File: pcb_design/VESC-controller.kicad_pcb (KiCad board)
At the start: 4 copper layers, 160 x 90 mm, 319 parts, among them J1 GATE_DRIVER_CONN_U, J2 GATE_DRIVER_CONN_V, J3 GATE_DRIVER_CONN_W, J4 micro USB, J5 ACCEL, J6 REGEN, J7 12V, J8 V_BUS, J9 SWD, P1 HALL/Encoder, P101 CANBUS, P2 Resolver, P3 PWR_COMM, Q1 BSC340N08, Q2 2N7002PW, Q3 AO4805, SW1 BOOTLOADER, U1 STM32F40X_LQFP64, U10 LM2903-SO8, U11 LM3488, U12 OPA2376AID, U13 LM1117IMP-v.v, U14 OPA2376AID, U15 AD2S1205, U16 OPA2376AID, U17 LM2903-SO8, U18 AND3, U19 AD8397, U2 ISO1050, U20 APX809, U21 NCV78Mxx, U3 OPA2376AID, U4 LM2903-SO8, U5 7400-TSSOP, U6 SN74ACT08PWR, U7 SN74ACT08PWR, U8 SN74AUP1G74, U9 LM22676QTJ-5.0, X1 ABM3B - 8MHz, X2 ABM3B - 8MHz

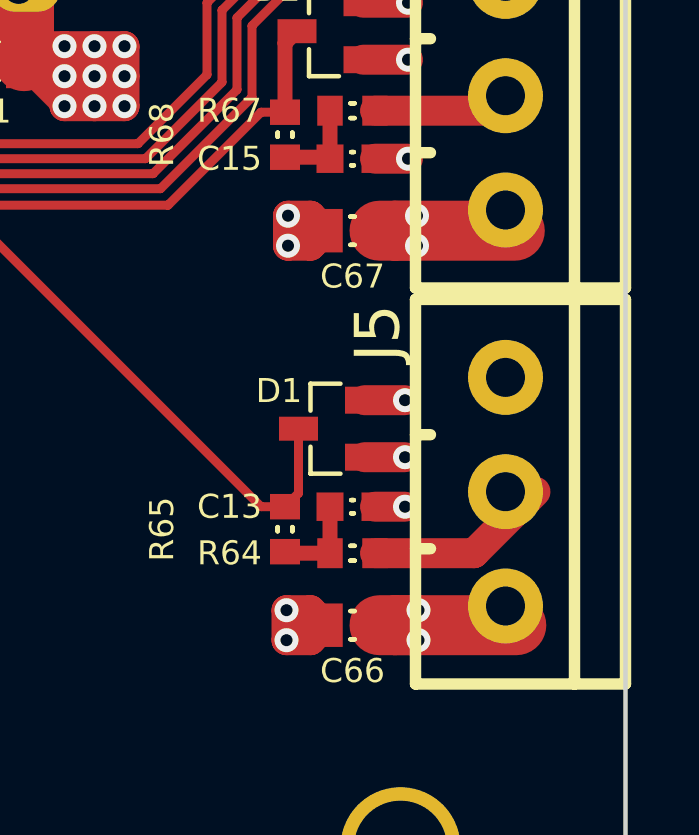
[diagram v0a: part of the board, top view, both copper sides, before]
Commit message: Updated component values according to simulations. 1.5khz for user inputs and  240khz lp pass filters for motor control
Signed-off-by: Marcos Chaparro <mchaparro@paltatech.com>
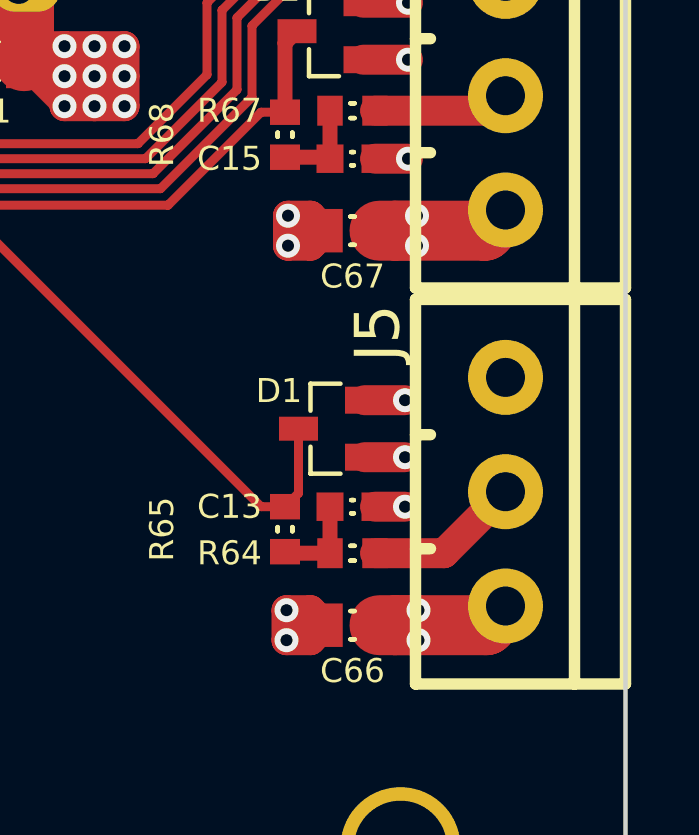
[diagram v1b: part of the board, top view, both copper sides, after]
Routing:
- net /Accel input conditioning/IN: track 6.20 -> 5.20 mm
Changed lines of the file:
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@@
     (thickness 1.6)
     (drawings 74)
-    (tracks 4755)
+    (tracks 4757)
     (zones 0)
     (modules 319)
@@
     (0 F.Cu signal)
     (1 GND.Cu signal)
-    (2 PWR.Cu signal hide)
+    (2 PWR.Cu signal)
     (31 B.Cu signal)
     (32 B.Adhes user)
@@
   )
   (setup
-    (last_trace_width 0.19)
+    (last_trace_width 2)
     (user_trace_width 0.2)
     (user_trace_width 0.25)
@@
   (segment (start 29.25 -1.95) (end 29.25 -2.925) (width 0.25) (layer F.Cu) (net 105))
   (segment (start 29.25 -2.925) (end 29.475 -3.15) (width 0.25) (layer F.Cu) (net 105))
-  (segment (start 71.65 27.7) (end 74.95 27.7) (width 1) (layer F.Cu) (net 106))
-  (segment (start 74.95 27.7) (end 77 25.65) (width 1) (layer F.Cu) (net 106))
+  (segment (start 71.65 27.7) (end 73.95 27.7) (width 1) (layer F.Cu) (net 106))
+  (segment (start 73.95 27.7) (end 76 25.65) (width 1) (layer F.Cu) (net 106))
   (segment (start 71.65 12.95) (end 76.5 12.95) (width 1) (layer F.Cu) (net 107))
   (segment (start 28.7 40.8) (end 28.7 38.475) (width 0.3) (layer F.Cu) (net 108) (status 10))
@@
   (segment (start 20.2 -36.8) (end 19.5 -36.1) (width 3) (layer F.Cu) (net 132))
   (segment (start 22.45 -34.2) (end 22.45 -36.8) (width 3) (layer F.Cu) (net 132))
+  (segment (start 71.8 30.1) (end 75.36 30.1) (width 2) (layer F.Cu) (net 133))
+  (segment (start 75.36 30.1) (end 76 29.46) (width 2) (layer F.Cu) (net 133))
+  (segment (start 71.8 16.95) (end 75.31 16.95) (width 2) (layer F.Cu) (net 133))
+  (segment (start 75.31 16.95) (end 76 16.26) (width 2) (layer F.Cu) (net 133))
   (segment (start 70.397745 -32.284414) (end 77.965586 -32.284414) (width 2) (layer F.Cu) (net 133))
   (segment (start 77.965586 -32.284414) (end 78.600001 -31.649999) (width 2) (layer F.Cu) (net 133))
@@
   (via (at 26.9 34.6) (size 0.8) (drill 0.4) (layers F.Cu B.Cu) (net 133))
   (via (at 27.9 34.6) (size 0.8) (drill 0.4) (layers F.Cu B.Cu) (net 133))
-  (segment (start 71.8 16.95) (end 76.31 16.95) (width 2) (layer F.Cu) (net 133))
-  (segment (start 71.8 30.1) (end 76.36 30.1) (width 2) (layer F.Cu) (net 133))
   (segment (start 73.05 16.45) (end 73.05 17.45) (width 1) (layer F.Cu) (net 133))
   (segment (start 73.05 16.45) (end 73.615685 16.45) (width 1) (layer PWR.Cu) (net 133))

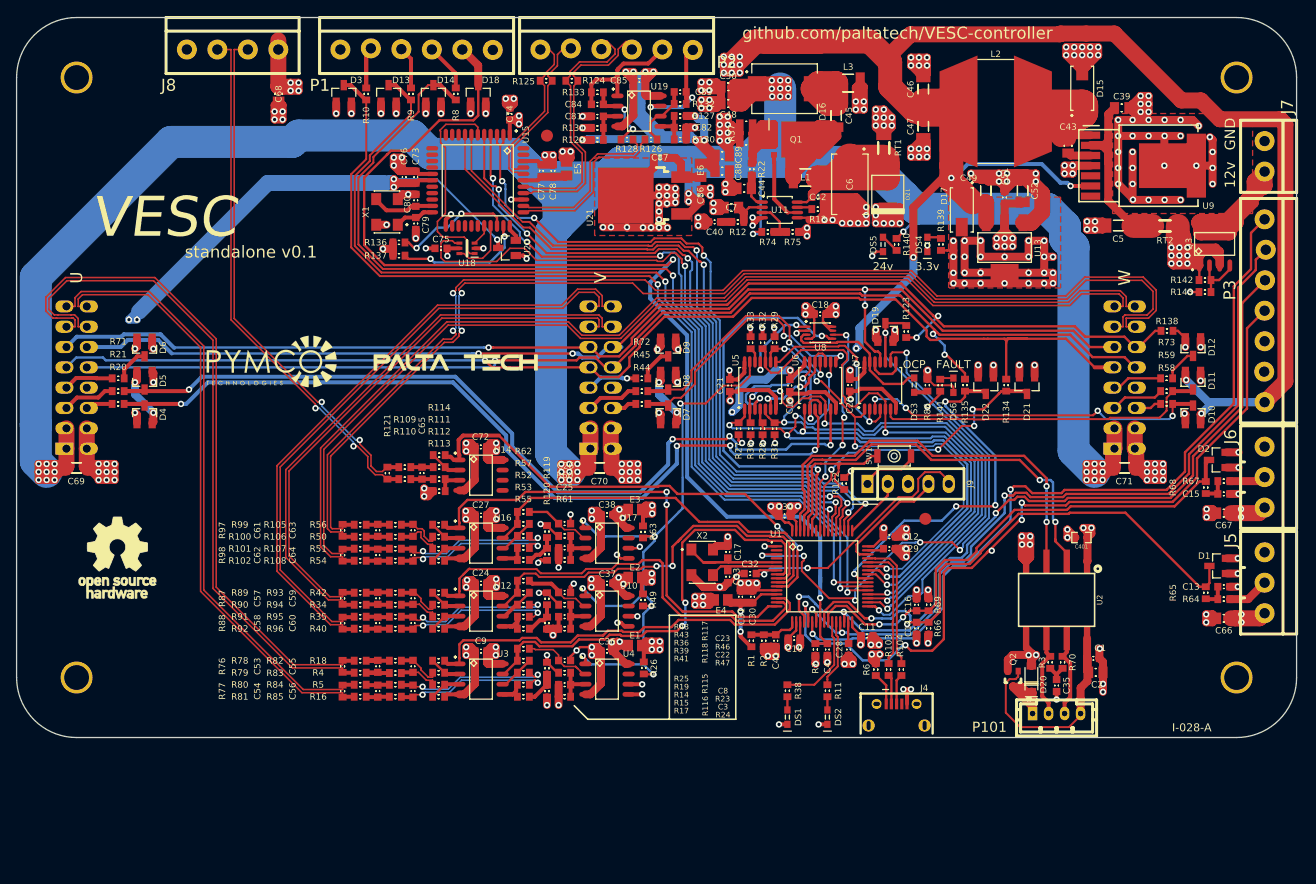
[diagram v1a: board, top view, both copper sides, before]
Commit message: Corrected phase current gain. More 3d models
Signed-off-by: Marcos Chaparro <mchaparro@paltatech.com>
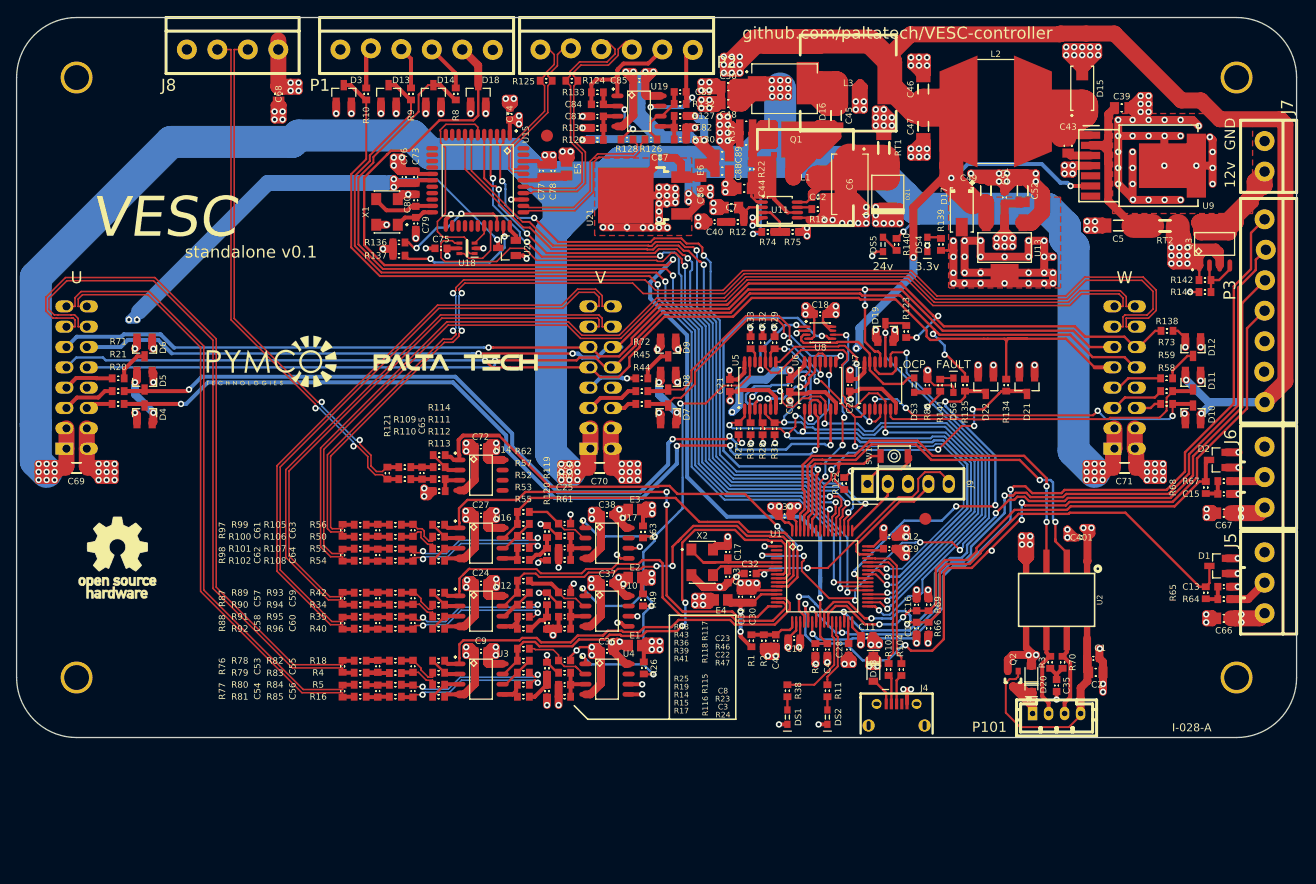
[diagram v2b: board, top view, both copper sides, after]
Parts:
- removed R6: 0R, IPC7351-Nominal:RESC1608X50
- added D23: MBR0540, smd-semi:SOD-123, F.Cu at (27.1, 36.4)
- C10, C11, C12, C34: value 2.2u -> 100nF
- C13, C15: value 1nF -> 100nF
- C17, C33, C79, C80: value 15p -> 15pF
- C2: value 10uF -> 4.7uF
- C28, C29, C31, C41: value 2.2u -> 2.2uF
- C32: value 100n -> 100nF
- C4: value 4.7nF -> 2.2uF
- C401: value 2.2u -> 100nF; footprint CRF1:SMD-0603_c -> IPC7351-Nominal:CAPC1608X55
- C5: value 10uF 50v -> 10uF 35v
- C53, C54, C57, C58, C61, C62: value 100pF -> 2.2nF
- C55, C56, C59, C60, C63, C64: value 100pF -> 220pF
- C6: value 4.7uF 50v -> 4.7uF 50v tant
- C76, C78: value 4.7uF -> 2.2uF
- E4: value BEAD-0805 -> BEAD-220ohm@100khz
- L1, L3: value L-1210 -> 22uH 5.2A; footprint IPC7351-Nominal:INDC3225X135 -> manuf:BOURNS-SRR1210
- R105, R106, R107, R108, R64, R67, R82, R83, R84, R85, R93, R94, R95, R96: value 100R -> 1k
- R109, R110: value 100R -> 4.7k
- R124, R125: value 68k -> 68.1k
- R14, R15, R34, R35, R36, R39, R4, R5, R50, R51, R52, R53: value 10k -> 8.87k
- R16, R40, R54: value R-0603 -> 10k
- R17, R41, R55: value 9.5k -> 10k
- R3, R70: value 120R -> 60.4R
- R65, R68: value 5.2k -> 100k
- R66, R69: value 10k -> 270k
- RT1: value POLYFUSE 5A -> FUSE 5A SLOW
- RT2: value POLYFUSE- 2A -> POLYFUSE 1A
- SW1: footprint paltatech:SMD-Switch_B3U-1000-B -> SMD-Switch_B3U-1000-B
- U10, U17, U4: value LM2903-SO8 -> LM2903DT
- U12, U14, U16, U3: value OPA2376AID -> OPA2376AIDR
- U18: value AND3 -> SN74LVC1G
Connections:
- net /conditioning U/OC_Fault renamed /conditioning U/~OC_Fault
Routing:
- net +5: track 682.1 -> 437.3 mm, vias 41 -> 27
- net GND: track 724.7 -> 951.5 mm, vias 286 -> 296
- net (no net): track 0.00 -> 12.5 mm, vias 0 -> 4
- net Net-(C45-Pad2): track 40.0 -> 48.0 mm
- net Net-(Q1-Pad4): track 9.16 -> 1.18 mm
- net Net-(C42-Pad1): track 25.3 -> 29.2 mm
- net Net-(D23-Pad2): track 4.13 -> 3.59 mm

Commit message: Fixed power supply inductor footprints in the layout
Signed-off-by: Marcos Chaparro <mchaparro@paltatech.com>
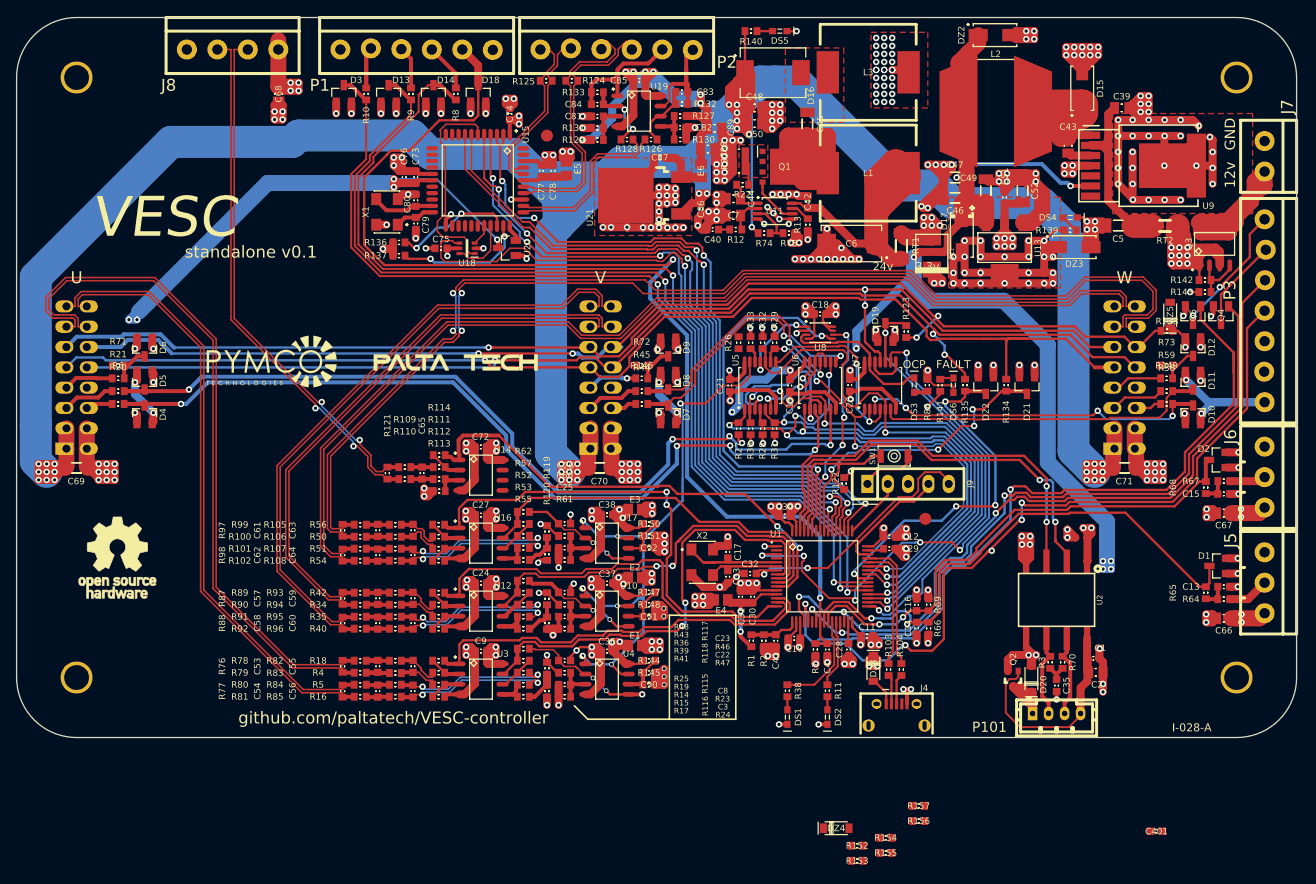
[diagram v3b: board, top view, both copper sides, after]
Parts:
- removed R49, R63: 4.7k, IPC7351-Nominal:RESC1608X50
- added C90: 100nF, IPC7351-Nominal:CAPC1608X55, F.Cu at (-0.95, 38.4)
- added C91: 100nF, IPC7351-Nominal:CAPC1608X55, F.Cu at (-0.95, 29.9)
- added C92: 100nF, IPC7351-Nominal:CAPC1608X55, F.Cu at (-0.95, 21.3)
- added DZ2: 5.7v zener, IPC7351-Nominal:DIOM5226X203, F.Cu at (42.3, -42.8)
- added DZ3: 4v zener, IPC7351-Nominal:DIOM5226X203, F.Cu at (52.2, -16.3)
- added DZ4: MMSZ52XXB, smd-semi:SOD-123, F.Cu at (22.4, 56.3)
- added DZ5: MMSZ52XXB, smd-semi:SOD-123, F.Cu at (64.2, -7.80)
- added Q4: SI2302, smd-semi:SOT-23, F.Cu at (70.5, -7.80)
- added Q5: SI2302, smd-semi:SOT-23, F.Cu at (67.0, -7.80)
- added R144: 10k, IPC7351-Nominal:RESC1608X50, F.Cu at (-0.95, 35.4)
- added R145: 1k, IPC7351-Nominal:RESC1608X50, F.Cu at (-0.95, 36.9)
- added R146: 10k, IPC7351-Nominal:RESC1608X50, F.Cu at (-1.85, -1.50)
- added R147: 10k, IPC7351-Nominal:RESC1608X50, F.Cu at (-0.95, 26.9)
- added R148: 1k, IPC7351-Nominal:RESC1608X50, F.Cu at (-0.95, 28.4)
- added R149: 10k, IPC7351-Nominal:RESC1608X50, F.Cu at (63.8, -1.50)
- added R150: 10k, IPC7351-Nominal:RESC1608X50, F.Cu at (-0.95, 18.3)
- added R151: 1k, IPC7351-Nominal:RESC1608X50, F.Cu at (-0.95, 19.8)
- added R152: 1k, IPC7351-Nominal:RESC1608X50, F.Cu at (25.1, 58.5)
- added R153: 1k, IPC7351-Nominal:RESC1608X50, F.Cu at (25.1, 60.4)
- added R154: NI, IPC7351-Nominal:RESC1608X50, F.Cu at (28.6, 57.5)
- added R155: NI, IPC7351-Nominal:RESC1608X50, F.Cu at (28.6, 59.4)
- added R156: NI, IPC7351-Nominal:RESC1608X50, F.Cu at (32.8, 55.4)
- added R157: NI, IPC7351-Nominal:RESC1608X50, F.Cu at (32.8, 53.5)
- added R6: 10k, IPC7351-Nominal:RESC1608X50, F.Cu at (-67.3, -1.50)
- DS5: value RED -> GREEN
- R113, R114: value 10k -> 22k
- R14, R15, R36, R39, R52, R53: value 8.87k -> 10k
- R17, R19, R41, R43, R55, R57: value 10k -> 8.87k
- R34, R35, R4, R5, R50, R51: value 8.87k -> 5.6k
- SW1: footprint SMD-Switch_B3U-1000-B -> paltatech:SMD-Switch_B3U-1000-B
- moved R26 42.3 mm to (10.2, -4.35), turned to 270 degrees
- moved C401 37.9 mm to (62.5, 56.7), turned to 0 degrees
- moved R140 32.3 mm to (11.8, -43.3), turned to 180 degrees
- moved DS5 29.6 mm to (15.4, -43.3), turned to 180 degrees
- moved DS4 18.2 mm to (51.7, -20.0), turned to 180 degrees
- moved R139 16.2 mm to (51.7, -18.4), turned to 180 degrees
- moved C46 14.2 mm to (37.3, -22.4), turned to 180 degrees
- moved RT1 12.4 mm to (30.6, -16.4)
- moved DZ1 9.21 mm to (34.4, -15.5)
- moved L1 7.87 mm to (26.4, -25.6)
- moved C47 7.53 mm to (37.3, -25.0), turned to 180 degrees
- moved C6 7.40 mm to (24.4, -16.8), turned to 180 degrees
- moved C50 5.66 mm to (12.2, -31.8), turned to 0 degrees
- moved C45 3.75 mm to (18.9, -31.7)
- moved Q1 3.69 mm to (16.0, -26.4)
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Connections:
- net /conditioning U/Power_good renamed /conditioning U/TEMP_G
- net /conditioning V/Power_good renamed /conditioning V/TEMP_G
- net /conditioning W/Power_good renamed /conditioning W/TEMP_G
- D12 pad 3: Net-(D12-Pad3) -> /conditioning W/TEMP
- D6 pad 3: Net-(D6-Pad3) -> /conditioning U/TEMP
- D9 pad 3: Net-(D9-Pad3) -> /conditioning V/TEMP
- DZ1 pad 1: Net-(C42-Pad1) -> Net-(DZ1-Pad1)
- P3 pad 1: /STM32F4/MISO_ADC_EXT2 -> /Protected GPIOs/OUT2
- P3 pad 2: /STM32F4/TX_SCL_MOSI -> /Protected GPIOs/OUT1
- P3 pad 3: /STM32F4/RX_SDA_NSS -> /STM32F4/TX_SCL_MOSI
- P3 pad 4: /STM32F4/SCK_ADC_EXT -> /STM32F4/RX_SDA_NSS
- Q3 pad 1: Net-(Q3-Pad1) -> Net-(DZ1-Pad1)
- Q3 pad 3: Net-(Q3-Pad1) -> Net-(DZ1-Pad1)
- R100 pad 2: /conditioning W/V_phase- -> /conditioning W/V_phase+
- R101 pad 2: /conditioning W/I_phase+ -> /conditioning W/I_phase-
- R102 pad 2: /conditioning W/I_phase- -> /conditioning W/I_phase+
- R109 pad 2: /V_bus+ -> /V_bus-
- R110 pad 2: /V_bus- -> /V_bus+
- R121 pad 1: /V_bus- -> /V_bus+
- R121 pad 2: /V_bus+ -> /V_bus-
- R142 pad 2: Net-(Q3-Pad1) -> Net-(DZ1-Pad1)
- R26 pad 1: /conditioning U/~OC_Fault -> +3.3
- R26 pad 2: +3.3 -> /conditioning U/~OC_Fault
- R71 pad 1: Net-(D6-Pad3) -> /conditioning U/TEMP
- R72 pad 1: Net-(D9-Pad3) -> /conditioning V/TEMP
- R73 pad 1: Net-(D12-Pad3) -> /conditioning W/TEMP
- R76 pad 1: /conditioning U/V_phase- -> /conditioning U/V_phase+
- R76 pad 2: /conditioning U/V_phase+ -> /conditioning U/V_phase-
- R77 pad 1: /conditioning U/I_phase- -> /conditioning U/I_phase+
- R77 pad 2: /conditioning U/I_phase+ -> /conditioning U/I_phase-
- R78 pad 2: /conditioning U/V_phase+ -> /conditioning U/V_phase-
- R79 pad 2: /conditioning U/V_phase- -> /conditioning U/V_phase+
- R80 pad 2: /conditioning U/I_phase+ -> /conditioning U/I_phase-
- R81 pad 2: /conditioning U/I_phase- -> /conditioning U/I_phase+
- R87 pad 1: /conditioning V/V_phase- -> /conditioning V/V_phase+
- R87 pad 2: /conditioning V/V_phase+ -> /conditioning V/V_phase-
- R88 pad 1: /conditioning V/I_phase- -> /conditioning V/I_phase+
- R88 pad 2: /conditioning V/I_phase+ -> /conditioning V/I_phase-
- R89 pad 2: /conditioning V/V_phase+ -> /conditioning V/V_phase-
- R90 pad 2: /conditioning V/V_phase- -> /conditioning V/V_phase+
- R91 pad 2: /conditioning V/I_phase+ -> /conditioning V/I_phase-
- R92 pad 2: /conditioning V/I_phase- -> /conditioning V/I_phase+
- R97 pad 1: /conditioning W/V_phase- -> /conditioning W/V_phase+
- R97 pad 2: /conditioning W/V_phase+ -> /conditioning W/V_phase-
- R98 pad 1: /conditioning W/I_phase- -> /conditioning W/I_phase+
- R98 pad 2: /conditioning W/I_phase+ -> /conditioning W/I_phase-
- R99 pad 2: /conditioning W/V_phase+ -> /conditioning W/V_phase-
- RT1 pad 2: Net-(Q3-Pad1) -> Net-(DZ1-Pad1)
- RT2 pad 2: Net-(Q3-Pad1) -> Net-(DZ1-Pad1)
- U1 pad 20: /STM32F4/RX_SDA_NSS -> /conditioning U/TEMP
- U1 pad 21: /STM32F4/SCK_ADC_EXT -> /conditioning V/TEMP
- U1 pad 22: /STM32F4/MISO_ADC_EXT2 -> /conditioning W/TEMP
- U1 pad 23: /STM32F4/TX_SCL_MOSI -> /Protected GPIOs/IN2
- U1 pad 58: /STM32F4/PWM_AUX -> /Protected GPIOs/IN1
- U10 pad 5: GND -> Net-(C23-Pad1)
- U10 pad 6: +3.3 -> Net-(C91-Pad1)
- U10 pad 7: Net-(U10-Pad7) -> /conditioning U/~OC_Fault
- U17 pad 5: GND -> Net-(C26-Pad1)
- U17 pad 6: +3.3 -> Net-(C92-Pad1)
- U17 pad 7: Net-(U17-Pad7) -> /conditioning U/~OC_Fault
- U4 pad 5: GND -> Net-(C8-Pad1)
- U4 pad 6: +3.3 -> Net-(C90-Pad1)
- U4 pad 7: Net-(U4-Pad7) -> /conditioning U/~OC_Fault
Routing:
- net GND: track 951.5 -> 745.6 mm, vias 296 -> 325
- net +5: track 437.3 -> 636.7 mm, vias 27 -> 36
- net Net-(DZ1-Pad1): track 0.00 -> 108.8 mm, vias 0 -> 14
- net Net-(Q3-Pad1): track 100.3 -> 0.00 mm, vias 17 -> 0
- net /STM32F4/MISO_ADC_EXT2: track 98.0 -> 0.00 mm, vias 2 -> 0
- net /Protected GPIOs/IN2: track 0.00 -> 87.4 mm, vias 0 -> 1
- net +24: track 410.9 -> 459.6 mm, vias 40 -> 36
- net Net-(Q1-Pad1): track 25.0 -> 3.12 mm
- net /conditioning V/3.3V_AN: track 39.5 -> 57.6 mm
- net /Protected GPIOs/OUT2: track 0.00 -> 16.8 mm, vias 0 -> 2
- net (no net): track 12.5 -> 0.00 mm, vias 4 -> 0
- net /conditioning U/3.3V_AN: track 48.8 -> 60.7 mm
- net +3.3: track 191.3 -> 179.6 mm, vias 76 -> 71
- net /Protected GPIOs/OUT1: track 0.00 -> 11.6 mm
- net Net-(C8-Pad1): track 9.10 -> 20.2 mm, vias 0 -> 3
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- added copper zone on F.Cu, net Net-(C45-Pad1)
- added copper zone on F.Cu, net Net-(Q1-Pad1)
